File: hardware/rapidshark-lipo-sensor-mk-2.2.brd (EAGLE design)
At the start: 35.6 x 20.3 mm, 13 parts, among them IC1 Tiny84, Q1 2N7000, Q2 2N7000, Q3 2N7000

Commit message: lipo voltage testing boards
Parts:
- removed Q1, Q2, Q3: 2N7000, a_parts:TO-92
- added C1, C2, C3: 100n, A_butts:C025-024X044
- added R5, R6: 10k, A_butts:RESISTOR-AXIAL-PTH-5.08MM
- BATT: value M04JST_XH_VERT -> M04PTH; device a_parts:JST-4-XH-VERT-TH -> a_parts:1X04-PTH-VERT
- moved AVRISP 12.6 mm to (26.7, 10.2), turned to 90 degrees
- moved C0 8.98 mm to (24.1, 3.81), turned to 90 degrees
- moved R0 8.03 mm to (24.1, 10.2)
- moved IC1 7.62 mm to (17.8, 10.2)
- moved R1 4.84 mm to (8.89, 1.91), turned to 0 degrees
- moved R2 3.70 mm to (8.89, 5.71)
- moved R3 3.70 mm to (8.89, 8.26), turned to 0 degrees
- moved R4 2.69 mm to (8.89, 12.1)
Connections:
- removed net EN1: IC1.2, Q1.2
- removed net EN2: IC1.3, Q2.2
- removed net EN3: IC1.5, Q3.2
- removed net N$3: Q3.3, R4.P$1
- net BATT-: now also C1.2, R1.P$1; no longer R1.P$2
- net CELL1+: now also C2.2, R3.P$1
- net CELL2+: now also C3.2, R4.P$2, R5.P$1; no longer R3.P$2
- net CELL3+: now also R6.P$2; no longer R4.P$2
- net VDIV1: now also C1.1, R1.P$2, R2.P$1; no longer Q1.1, R1.P$1
- net VDIV2: now also C2.1, R3.P$2, R4.P$1; no longer Q1.3, Q2.1, R2.P$1
- net VDIV3: now also C3.1, R5.P$2, R6.P$1; no longer Q2.3, Q3.1, R3.P$1
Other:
- board size 35.6 x 20.3 mm -> 33 x 20.3 mm

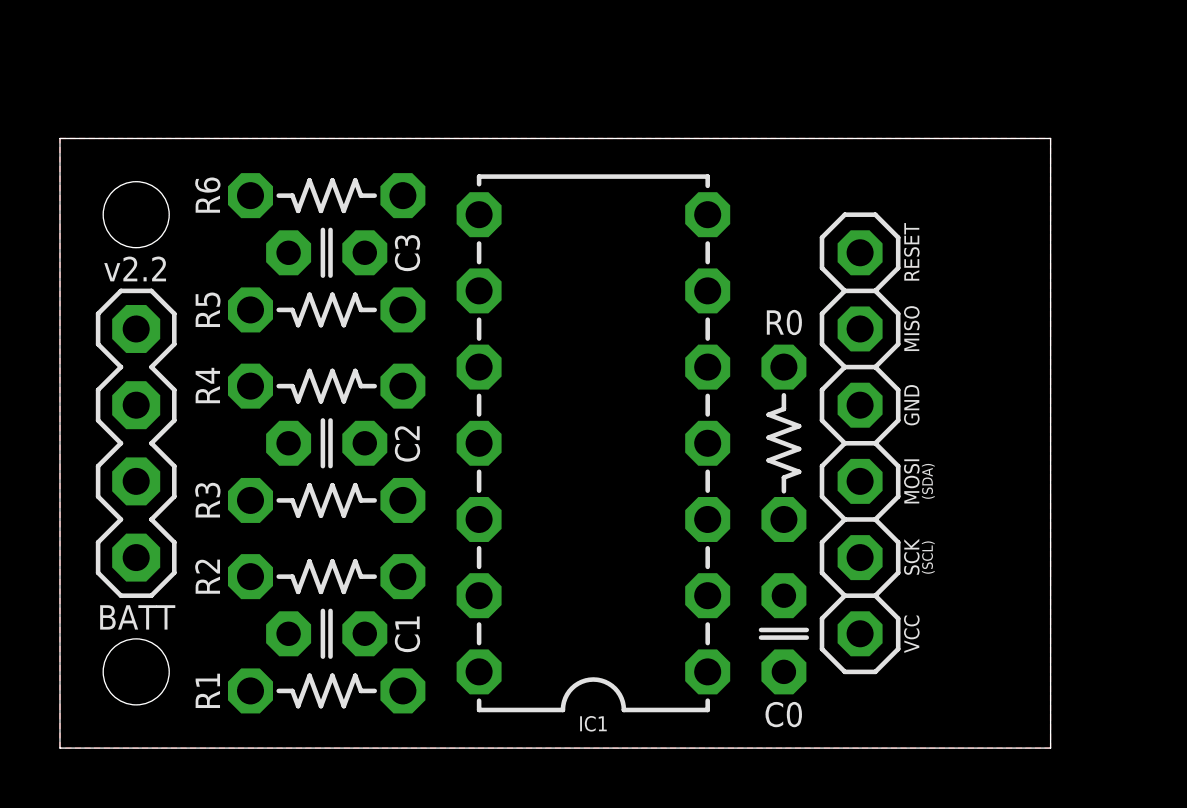
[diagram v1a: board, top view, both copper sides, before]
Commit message: unfinished hardware design for a battery level tester which reports over SPI/I2c
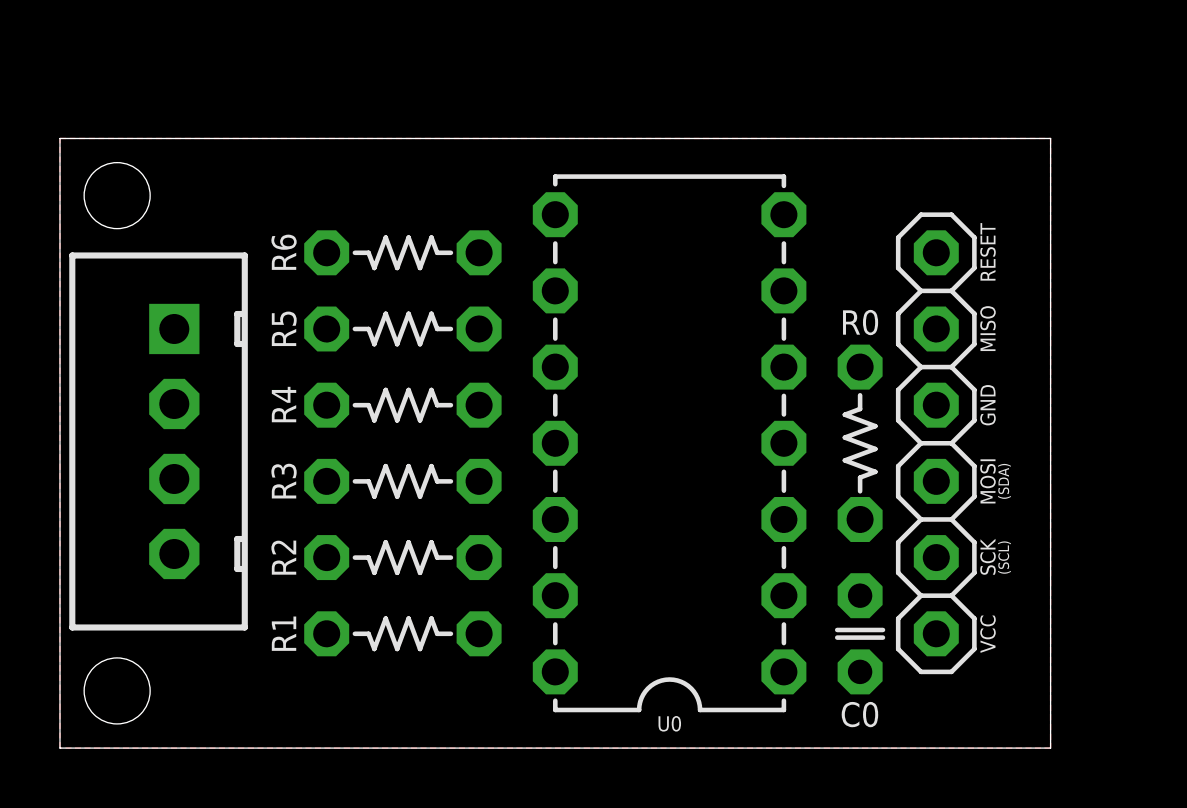
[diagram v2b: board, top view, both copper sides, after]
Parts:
- removed C1, C2, C3: 100n, A_butts:C025-024X044
- removed IC1: Tiny84, A_butts:DIL14
- added U0: Tiny84, A_butts:DIL14
- BATT: value M04PTH -> M04JST_XH_VERT; device a_parts:1X04-PTH-VERT -> a_parts:JST-4-XH-VERT-TH
- moved BATT 7.73 mm to (3.81, 14.0), turned to 270 degrees
- moved R1 3.17 mm to (11.4, 3.81)
- moved R6 3.17 mm to (11.4, 16.5)
- moved R2 2.62 mm to (11.4, 6.35)
- moved R3 2.62 mm to (11.4, 8.89)
- moved R4 2.62 mm to (11.4, 11.4)
- moved R5 2.62 mm to (11.4, 14.0)
- moved C0 2.54 mm to (26.7, 3.81)
- moved R0 2.54 mm to (26.7, 10.2)
- moved AVRISP 2.54 mm to (29.2, 10.2)
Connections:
- removed net BATT-: BATT.1, C1.2, R1.P$1
- net CELL1+: now also BATT.3; no longer BATT.2, C2.2, R3.P$1
- net CELL2+: now also BATT.2; no longer BATT.3, C3.2, R5.P$1
- net CELL3+: now also BATT.1; no longer BATT.4
- net GND: now also BATT.4, R1.P$1, R3.P$1, R5.P$1, U0.14; no longer IC1.14
- net MISO: now also U0.8; no longer IC1.8
- net MOSI/SDA: now also U0.7; no longer IC1.7
- net RESET: now also U0.4; no longer IC1.4
- net SCK/SCL: now also U0.9; no longer IC1.9
- net VCC: now also U0.1; no longer IC1.1
- net VDIV1: now also U0.12; no longer C1.1, IC1.12
- net VDIV2: now also U0.11; no longer C2.1, IC1.11
- net VDIV3: now also U0.10; no longer C3.1, IC1.10
